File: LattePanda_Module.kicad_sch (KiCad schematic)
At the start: 10 parts, among them J78 Conn_01x03_Pin

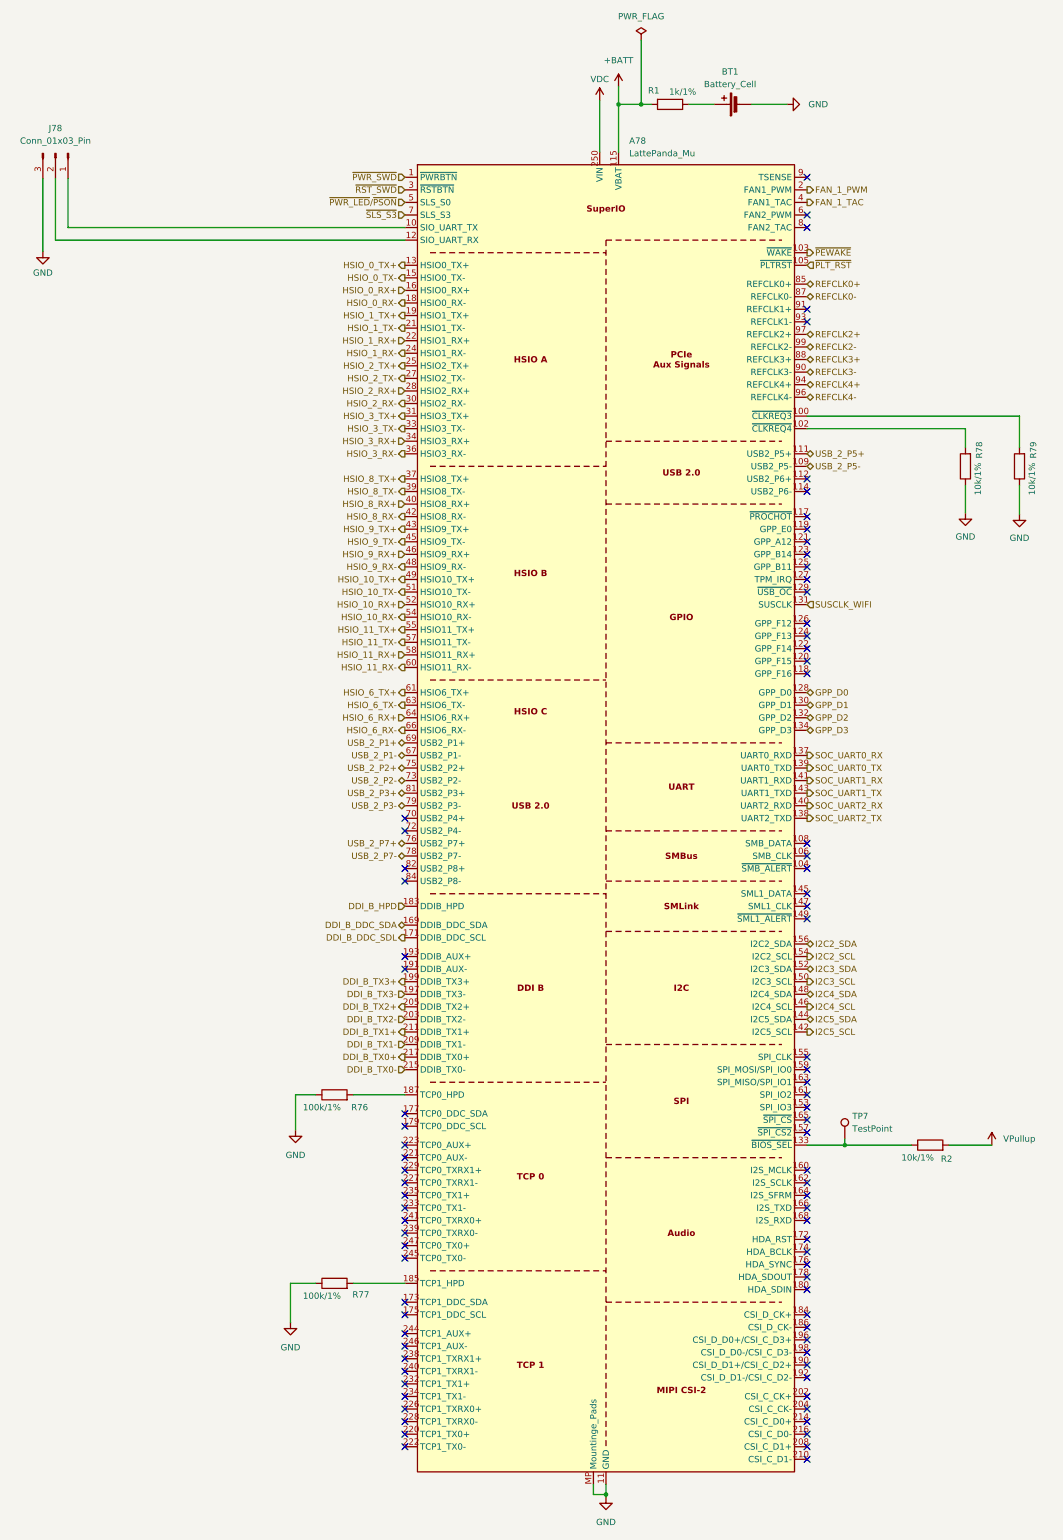
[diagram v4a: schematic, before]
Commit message: Fixed the Grid connection errors in the PSU Schematic sheet
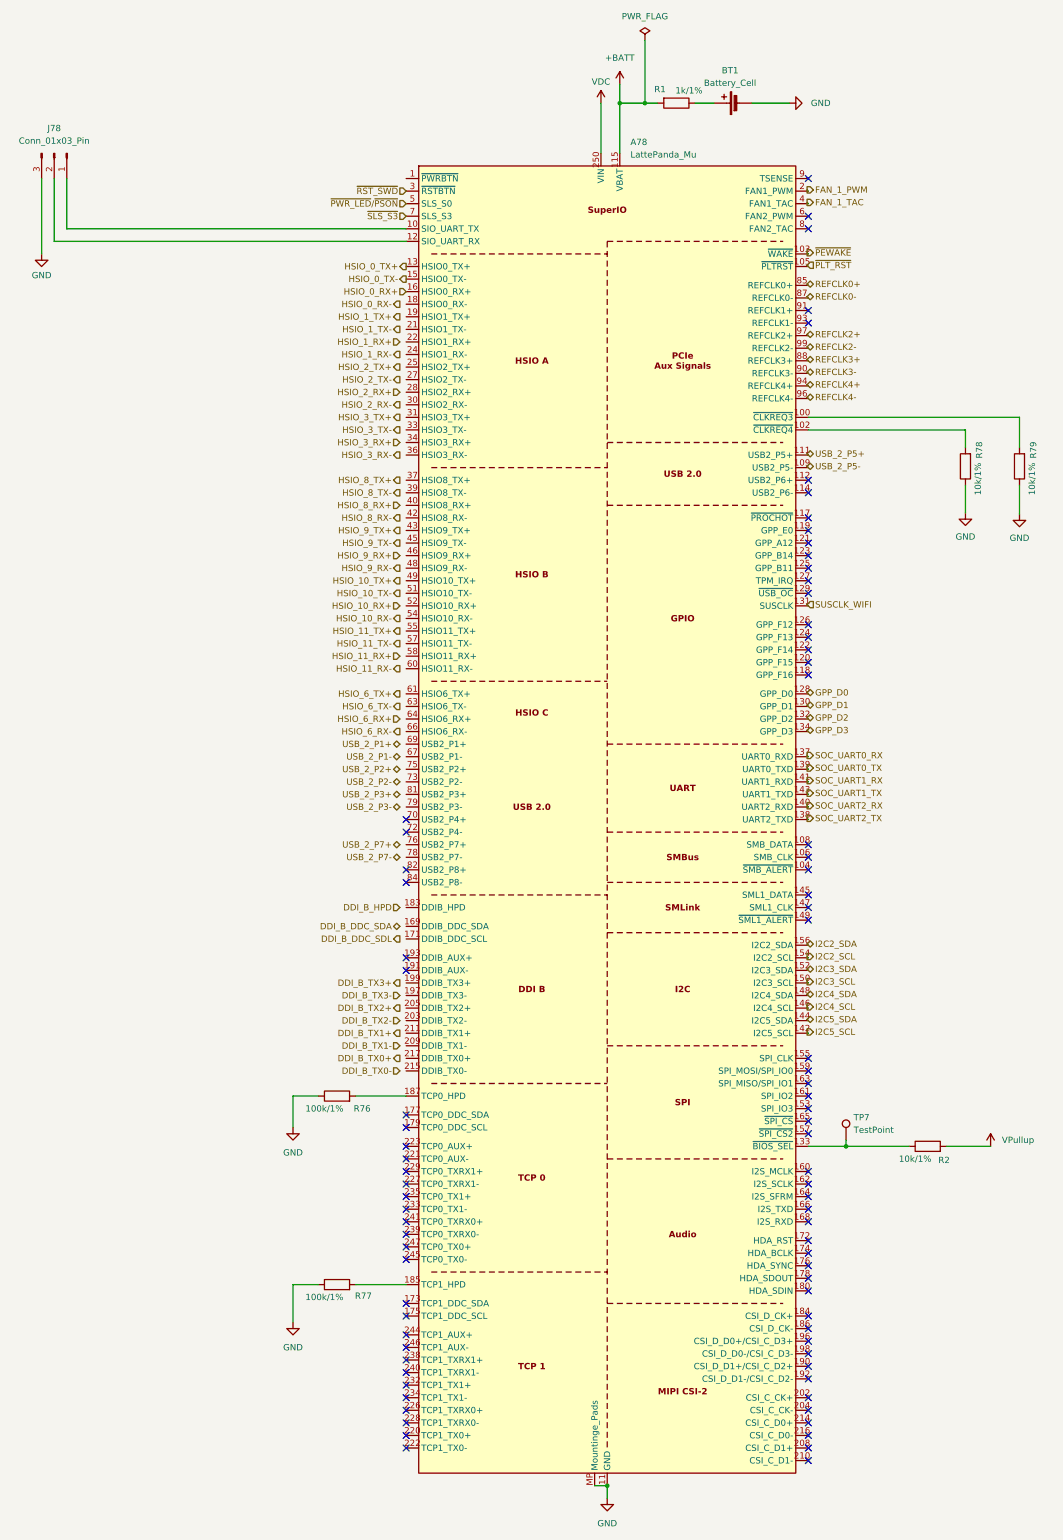
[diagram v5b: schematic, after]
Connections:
- net DDI_B_DDC_SDA: no longer A78.169 (DDIB_DDC_SDA)
- net DDI_B_DDC_SDL: no longer A78.171 (DDIB_DDC_SCL)
- net DDI_B_HPD: no longer A78.183 (DDIB_HPD)
- net DDI_B_TX0+: no longer A78.217 (DDIB_TX0+)
- net DDI_B_TX0-: no longer A78.215 (DDIB_TX0-)
- net DDI_B_TX1+: no longer A78.211 (DDIB_TX1+)
- net DDI_B_TX1-: no longer A78.209 (DDIB_TX1-)
- net DDI_B_TX2+: no longer A78.205 (DDIB_TX2+)
- net DDI_B_TX2-: no longer A78.203 (DDIB_TX2-)
- net DDI_B_TX3+: no longer A78.199 (DDIB_TX3+)
- net DDI_B_TX3-: no longer A78.197 (DDIB_TX3-)
- net HSIO_0_RX-: no longer A78.18 (HSIO0_RX-)
- net HSIO_10_RX+: no longer A78.52 (HSIO10_RX+)
- net HSIO_10_RX-: no longer A78.54 (HSIO10_RX-)
- net HSIO_10_TX+: no longer A78.49 (HSIO10_TX+)
- net HSIO_10_TX-: no longer A78.51 (HSIO10_TX-)
- net HSIO_11_RX+: no longer A78.58 (HSIO11_RX+)
- net HSIO_11_RX-: no longer A78.60 (HSIO11_RX-)
- net HSIO_11_TX+: no longer A78.55 (HSIO11_TX+)
- net HSIO_11_TX-: no longer A78.57 (HSIO11_TX-)
- net HSIO_1_RX+: no longer A78.22 (HSIO1_RX+)
- net HSIO_1_RX-: no longer A78.24 (HSIO1_RX-)
- net HSIO_1_TX+: no longer A78.19 (HSIO1_TX+)
- net HSIO_1_TX-: no longer A78.21 (HSIO1_TX-)
- net HSIO_2_RX+: no longer A78.28 (HSIO2_RX+)
- net HSIO_2_RX-: no longer A78.30 (HSIO2_RX-)
- net HSIO_2_TX+: no longer A78.25 (HSIO2_TX+)
- net HSIO_2_TX-: no longer A78.27 (HSIO2_TX-)
- net HSIO_3_RX+: no longer A78.34 (HSIO3_RX+)
- net HSIO_3_RX-: no longer A78.36 (HSIO3_RX-)
- net HSIO_3_TX+: no longer A78.31 (HSIO3_TX+)
- net HSIO_3_TX-: no longer A78.33 (HSIO3_TX-)
- net HSIO_6_RX+: no longer A78.64 (HSIO6_RX+)
- net HSIO_6_RX-: no longer A78.66 (HSIO6_RX-)
- net HSIO_6_TX+: no longer A78.61 (HSIO6_TX+)
- net HSIO_6_TX-: no longer A78.63 (HSIO6_TX-)
- net HSIO_8_RX+: no longer A78.40 (HSIO8_RX+)
- net HSIO_8_RX-: no longer A78.42 (HSIO8_RX-)
- net HSIO_8_TX+: no longer A78.37 (HSIO8_TX+)
- net HSIO_8_TX-: no longer A78.39 (HSIO8_TX-)
- net HSIO_9_RX+: no longer A78.46 (HSIO9_RX+)
- net HSIO_9_RX-: no longer A78.48 (HSIO9_RX-)
- net HSIO_9_TX+: no longer A78.43 (HSIO9_TX+)
- net HSIO_9_TX-: no longer A78.45 (HSIO9_TX-)
- net USB_2_P1+: no longer A78.69 (USB2_P1+)
- net USB_2_P1-: no longer A78.67 (USB2_P1-)
- net USB_2_P2+: no longer A78.75 (USB2_P2+)
- net USB_2_P2-: no longer A78.73 (USB2_P2-)
- net USB_2_P3+: no longer A78.81 (USB2_P3+)
- net USB_2_P3-: no longer A78.79 (USB2_P3-)
- net USB_2_P7+: no longer A78.76 (USB2_P7+)
- net USB_2_P7-: no longer A78.78 (USB2_P7-)
- net ~{PWR_SWD}: no longer names the net of A78.1 (~{PWRBTN})
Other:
- moved on the sheet: R1, R2, R76, R77

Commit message: Wired the hierichal sheets together for the PSU and the main MU Module
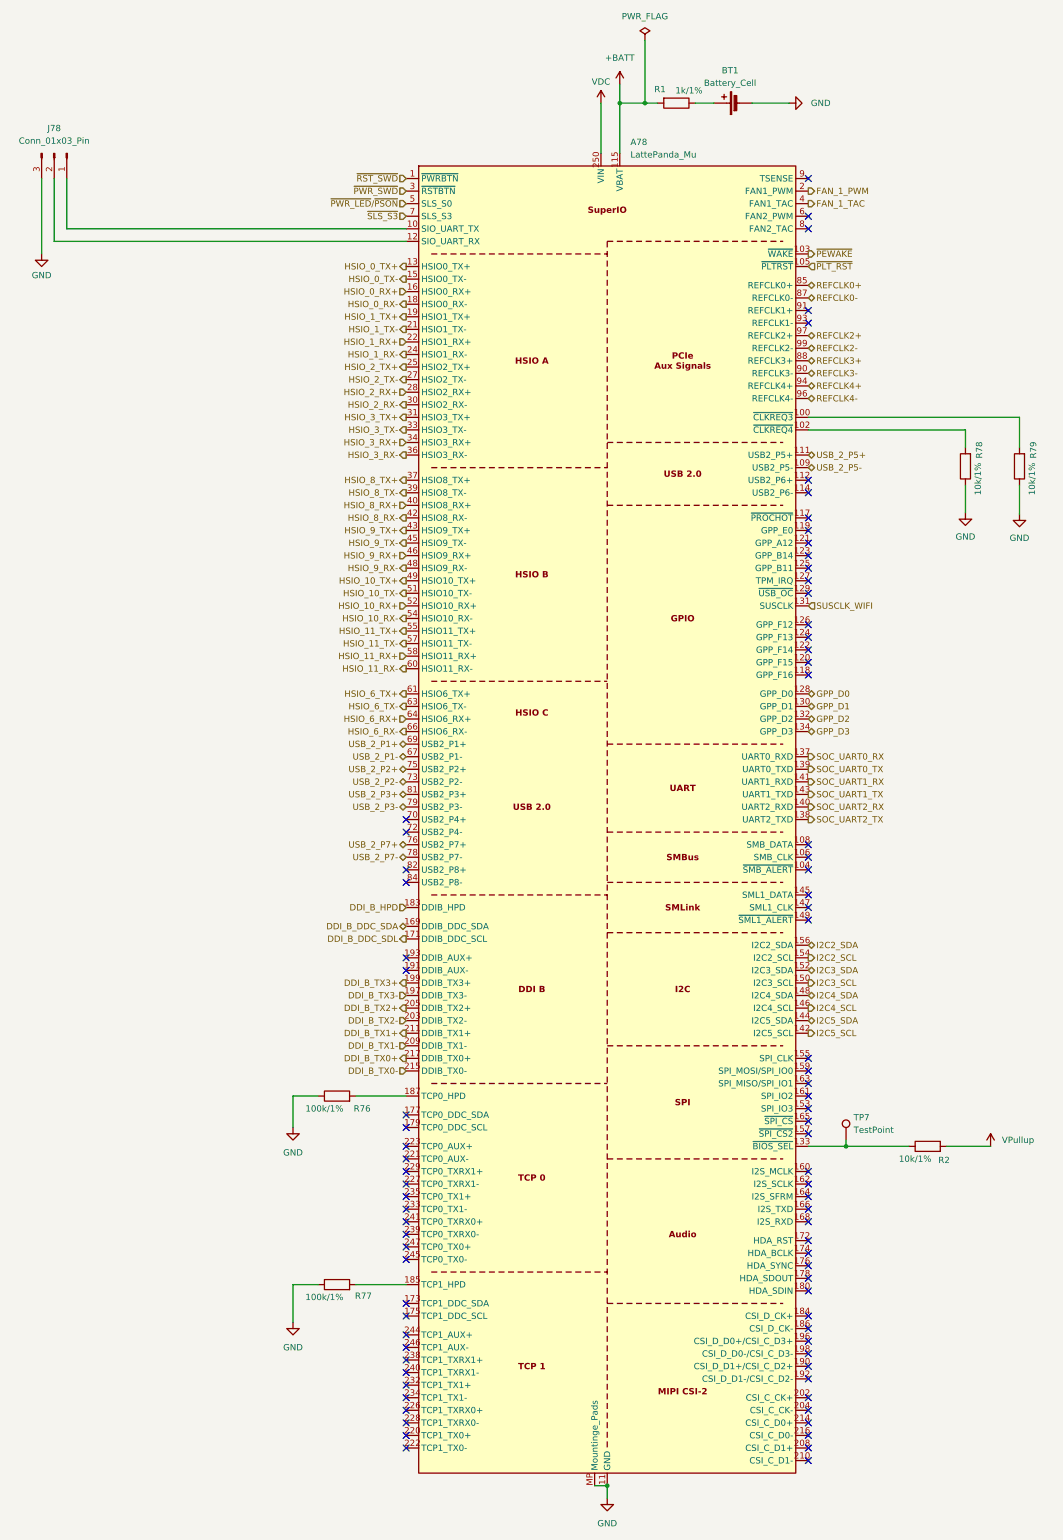
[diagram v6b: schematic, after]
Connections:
- net DDI_B_DDC_SDA: now also A78.169 (DDIB_DDC_SDA)
- net DDI_B_DDC_SDL: now also A78.171 (DDIB_DDC_SCL)
- net DDI_B_HPD: now also A78.183 (DDIB_HPD)
- net DDI_B_TX0+: now also A78.217 (DDIB_TX0+)
- net DDI_B_TX0-: now also A78.215 (DDIB_TX0-)
- net DDI_B_TX1+: now also A78.211 (DDIB_TX1+)
- net DDI_B_TX1-: now also A78.209 (DDIB_TX1-)
- net DDI_B_TX2+: now also A78.205 (DDIB_TX2+)
- net DDI_B_TX2-: now also A78.203 (DDIB_TX2-)
- net DDI_B_TX3+: now also A78.199 (DDIB_TX3+)
- net DDI_B_TX3-: now also A78.197 (DDIB_TX3-)
- net HSIO_0_RX-: now also A78.18 (HSIO0_RX-)
- net HSIO_10_RX+: now also A78.52 (HSIO10_RX+)
- net HSIO_10_RX-: now also A78.54 (HSIO10_RX-)
- net HSIO_10_TX+: now also A78.49 (HSIO10_TX+)
- net HSIO_10_TX-: now also A78.51 (HSIO10_TX-)
- net HSIO_11_RX+: now also A78.58 (HSIO11_RX+)
- net HSIO_11_RX-: now also A78.60 (HSIO11_RX-)
- net HSIO_11_TX+: now also A78.55 (HSIO11_TX+)
- net HSIO_11_TX-: now also A78.57 (HSIO11_TX-)
- net HSIO_1_RX+: now also A78.22 (HSIO1_RX+)
- net HSIO_1_RX-: now also A78.24 (HSIO1_RX-)
- net HSIO_1_TX+: now also A78.19 (HSIO1_TX+)
- net HSIO_1_TX-: now also A78.21 (HSIO1_TX-)
- net HSIO_2_RX+: now also A78.28 (HSIO2_RX+)
- net HSIO_2_RX-: now also A78.30 (HSIO2_RX-)
- net HSIO_2_TX+: now also A78.25 (HSIO2_TX+)
- net HSIO_2_TX-: now also A78.27 (HSIO2_TX-)
- net HSIO_3_RX+: now also A78.34 (HSIO3_RX+)
- net HSIO_3_RX-: now also A78.36 (HSIO3_RX-)
- net HSIO_3_TX+: now also A78.31 (HSIO3_TX+)
- net HSIO_3_TX-: now also A78.33 (HSIO3_TX-)
- net HSIO_6_RX+: now also A78.64 (HSIO6_RX+)
- net HSIO_6_RX-: now also A78.66 (HSIO6_RX-)
- net HSIO_6_TX+: now also A78.61 (HSIO6_TX+)
- net HSIO_6_TX-: now also A78.63 (HSIO6_TX-)
- net HSIO_8_RX+: now also A78.40 (HSIO8_RX+)
- net HSIO_8_RX-: now also A78.42 (HSIO8_RX-)
- net HSIO_8_TX+: now also A78.37 (HSIO8_TX+)
- net HSIO_8_TX-: now also A78.39 (HSIO8_TX-)
- net HSIO_9_RX+: now also A78.46 (HSIO9_RX+)
- net HSIO_9_RX-: now also A78.48 (HSIO9_RX-)
- net HSIO_9_TX+: now also A78.43 (HSIO9_TX+)
- net HSIO_9_TX-: now also A78.45 (HSIO9_TX-)
- net USB_2_P1+: now also A78.69 (USB2_P1+)
- net USB_2_P1-: now also A78.67 (USB2_P1-)
- net USB_2_P2+: now also A78.75 (USB2_P2+)
- net USB_2_P2-: now also A78.73 (USB2_P2-)
- net USB_2_P3+: now also A78.81 (USB2_P3+)
- net USB_2_P3-: now also A78.79 (USB2_P3-)
- net USB_2_P7+: now also A78.76 (USB2_P7+)
- net USB_2_P7-: now also A78.78 (USB2_P7-)
- net ~{RST_SWD}: now also A78.1 (~{PWRBTN}); no longer A78.3 (~{RSTBTN})
- new net ~{PWR_SWD}: A78.3 (~{RSTBTN})

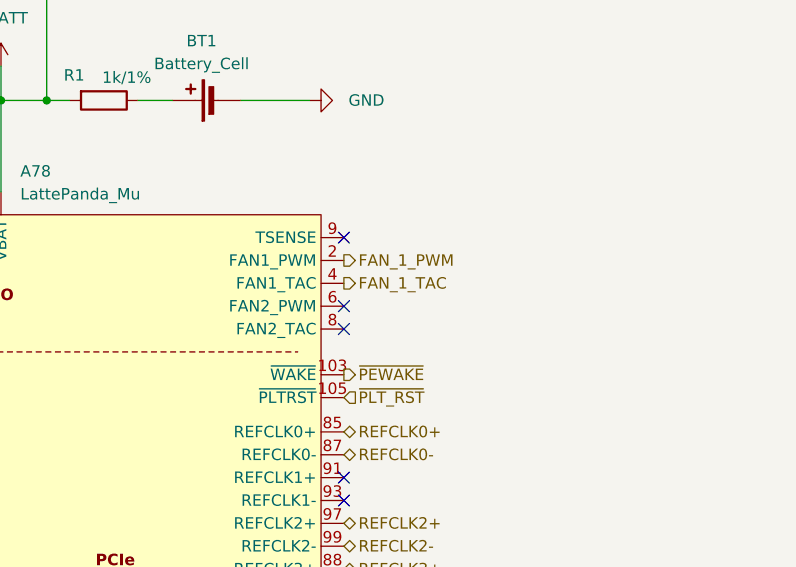
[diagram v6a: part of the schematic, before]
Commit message: Connected the hierarchal sheets together for the fan and the Mu moduls on the main sheet level and also added the label for the extrnal temp sensor for thermistor
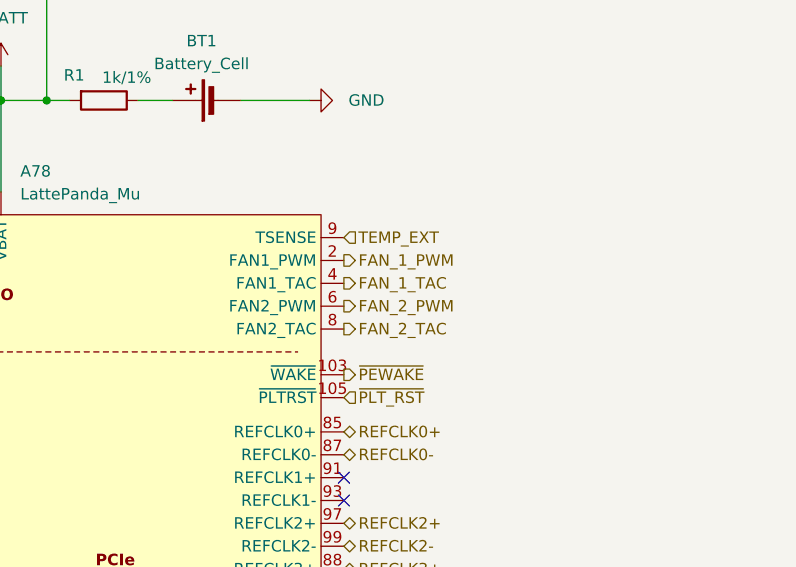
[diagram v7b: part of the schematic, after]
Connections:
- net FAN_2_PWM: now reaches A78.6 (FAN2_PWM)
- net FAN_2_TAC: now reaches A78.8 (FAN2_TAC)
- net TEMP_EXT: now reaches A78.9 (TSENSE)
- no-connect marks 84 -> 81
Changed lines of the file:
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@@
-	)
-	(no_connect
-		(at 332.74 81.28)
 	)
 	(no_connect
@@
 	)
 	(no_connect
-		(at 332.74 78.74)
-	)
-	(no_connect
 		(at 332.74 171.45)
 	)
@@
 	)
 	(no_connect
-		(at 332.74 71.12)
-	)
-	(no_connect
 		(at 251.46 200.66)
 	)
@@
 		)
 	)
+	(hierarchical_label "FAN_2_TAC"
+		(shape output)
+		(at 332.74 81.28 0)
+		(effects
+			(font
+				(size 1.27 1.27)
+			)
+			(justify left)
+		)
+	)
 	(hierarchical_label "REFCLK4+"
 		(shape bidirectional)
@@
 		)
 	)
+	(hierarchical_label "FAN_2_PWM"
+		(shape output)
+		(at 332.74 78.74 0)
+		(effects
+			(font
+				(size 1.27 1.27)
+			)
+			(justify left)
+		)
+	)
 	(hierarchical_label "SOC_UART1_RX"
 		(shape output)
@@
 		(effects
 			(font
+				(size 1.27 1.27)
+			)
+			(justify left)
+		)
+	)
+	(hierarchical_label "TEMP_EXT"
+		(shape input)
+		(at 332.74 71.12 0)
+		(effects
+			(font

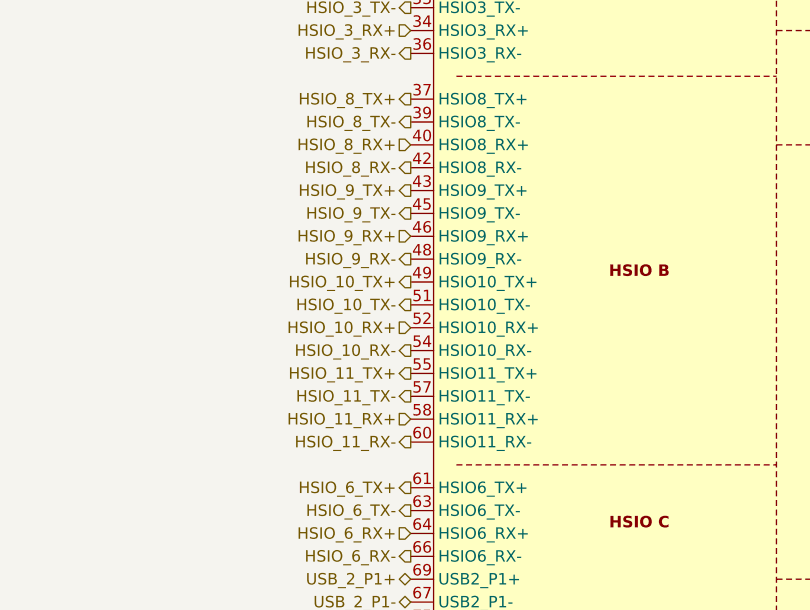
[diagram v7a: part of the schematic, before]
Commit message: Connected the hierchal labels to the main mu module in the root sheet
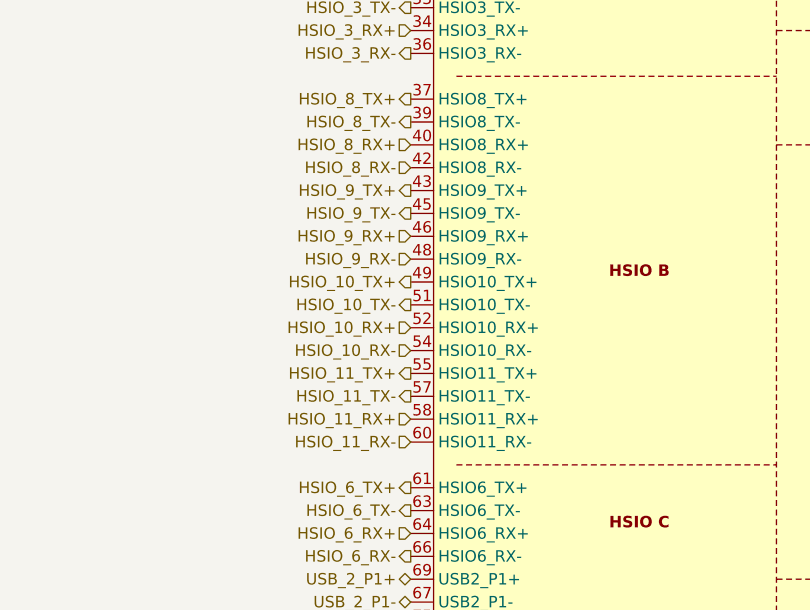
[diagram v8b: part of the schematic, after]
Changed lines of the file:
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@@
 	)
 	(hierarchical_label "HSIO_11_RX-"
-		(shape output)
+		(shape input)
 		(at 251.46 170.18 180)
 		(effects
@@
 	)
 	(hierarchical_label "HSIO_9_RX-"
-		(shape output)
+		(shape input)
 		(at 251.46 149.86 180)
 		(effects
@@
 	)
 	(hierarchical_label "HSIO_10_RX-"
-		(shape output)
+		(shape input)
 		(at 251.46 160.02 180)
 		(effects
@@
 	)
 	(hierarchical_label "HSIO_8_RX-"
-		(shape output)
+		(shape input)
 		(at 251.46 139.7 180)
 		(effects
